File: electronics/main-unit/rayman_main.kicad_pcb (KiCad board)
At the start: 2 copper layers, 88 x 100 mm, 112 parts, among them M1 M1, M2 M2, Q1 BC817, T1A_FUSE2 1808 SMD FUSEHOLDER, U1 ESP32-S3-WROOM-1, U2 SN74AHCT125N, U3 MCP1826S-3302E/DB, U4 SSR-DA41F

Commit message: lamp animation fix
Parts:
- removed AUDIO1: Conn_01x03_Socket, Connector_Audio:Jack_3.5mm_PJ320D_Horizontal
- removed the R21 at (103.6, 98.2)
- added AUDIO_OUT1: Conn_01x03_Socket, Connector_JST:JST_PH_B3B-PH-SM4-TB_1x03-1MP_P2.00mm_Vertical, F.Cu at (76.4, 83.6)
- added R33: 220R, Resistor_SMD:R_0805_2012Metric, B.Cu at (95.0, 36.6)
- added R34: 220R, Resistor_SMD:R_0805_2012Metric, B.Cu at (113.2, 66.7)
- R40: renamed from R29; value 1k -> 10k
- R41: renamed from R26; value 2k2 -> 22k
- moved R31 2.18 mm to (102.8, 98.2)
- moved R30 1.36 mm to (99.0, 98.2)
- moved R7 1.19 mm to (141.1, 36.4)
- moved C6 0.91 mm to (130.2, 38.0)
- moved C7 0.59 mm to (130.2, 35.5)
- renumbered C4 to C10, C5 to C11, C23 to C12, C24 to C13, C12 to C14, C22 to C15, C8 to C16, C9 to C17, C7 to C18, C16 to C19, C15 to C2, C17 to C20, C18 to C21, C19 to C22, C10 to C23, C11 to C24, C20 to C4, C2 to C5, C13 to C6, C14 to C7, C6 to C8, C21 to C9, D15 to D1, D8 to D10, D3 to D11, D11 to D12, D7 to D14, D12 to D15, D14 to D16, D16 to D2, D9 to D3, D10 to D4, D4 to D5, D5 to D7, D1 to D8, D2 to D9, R35 to R1, R14 to R12, R8 to R13, R15 to R14, R40 to R15, R12 to R16, R13 to R17, R42 to R18, R20 to R19, R7 to R2, R31 to R20, R32 to R21, R37 to R22, R3 to R23, R1 to R24, R38 to R25, R25 to R26, R39 to R27, R4 to R28, R24 to R29, R5 to R3, R17 to R30, R18 to R31, R19 to R32, R2 to R35, R28 to R36, R27 to R37, R16 to R38, R30 to R39, R36 to R4, R33 to R42, R34 to R43, R41 to R5, R22 to R6, R23 to R7, R6 to R8, T1A_FUSE2 to T1A_FUSE1, U4 to U3, U3 to U4
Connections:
- PROG1 pad MP: GND -> (no net)
- R19 pad 1: Net-(U1-IO14) -> Net-(U2-4A)
- RJ_LED1 pad 8: GND -> Net-(R33-Pad1)
- TF1 pad G1: GND -> unconnected-(TF1-PadG1)
- TF1 pad G2: GND -> unconnected-(TF1-PadG2)
- TF1 pad G3: GND -> unconnected-(TF1-PadG3)
- TF1 pad G4: GND -> unconnected-(TF1-PadG4)
- U1 pad 38: unconnected-(U1-IO2-Pad38) -> io2
- U2 pad 11: Net-(U2-4Y) -> unconnected-(U2-4Y-Pad11)
- U2 pad 12: Net-(U1-IO14) -> Net-(U2-4A)
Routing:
- net Net-(R33-Pad1): track 0.00 -> 122.4 mm, vias 0 -> 1
- net Net-(R34-Pad1): track 25.4 -> 77.5 mm, vias 0 -> 1
- net Net-(U1-IO14): track 58.7 -> 22.2 mm, vias 3 -> 2
- net Net-(U2-4Y): track 28.5 -> 0.00 mm
- net io2: track 0.00 -> 24.6 mm, vias 0 -> 2
- net Net-(U2-4A): track 0.00 -> 13.6 mm, vias 0 -> 1
- net Net-(DF_MUSIC1-DAC_L): track 63.1 -> 71.3 mm, vias 1 -> 0
- net Net-(audio_out1-DO): track 9.40 -> 14.7 mm
- net GND: track 65.9 -> 63.8 mm
- net Net-(U2-2Y): track 14.4 -> 13.2 mm
- net +3V3: track 306.6 -> 305.7 mm, vias 10 -> 9
- net Net-(R31-Pad2): track 35.0 -> 34.1 mm
- net Net-(TB1-BIN1): track 91.1 -> 90.4 mm
- net Net-(U2-1Y): track 10.3 -> 9.69 mm
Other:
- board text added: "Rev 1.5 25-MAR-2026"
- board text removed: "Rev 1.4 27-JAN-2026"

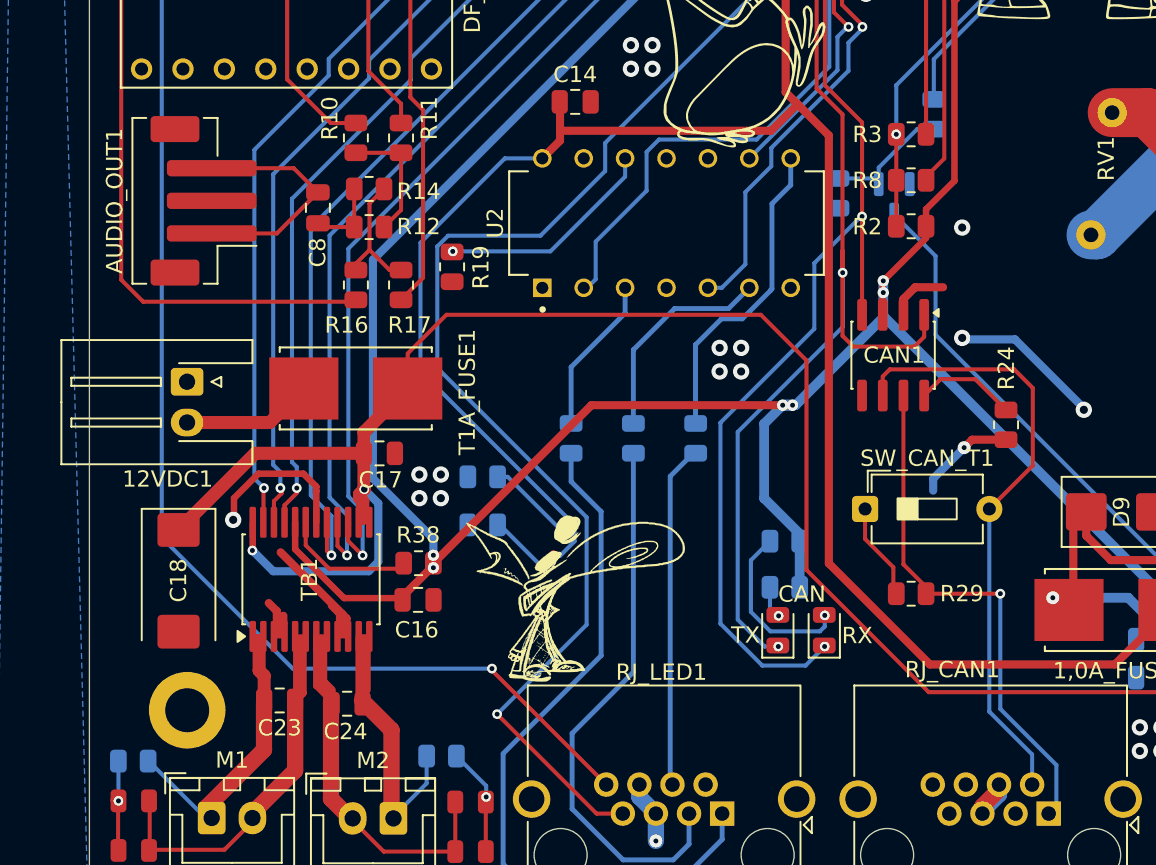
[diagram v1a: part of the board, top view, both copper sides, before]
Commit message: lamp fans control added; uv boost anims added; ambiente light timeout fixed
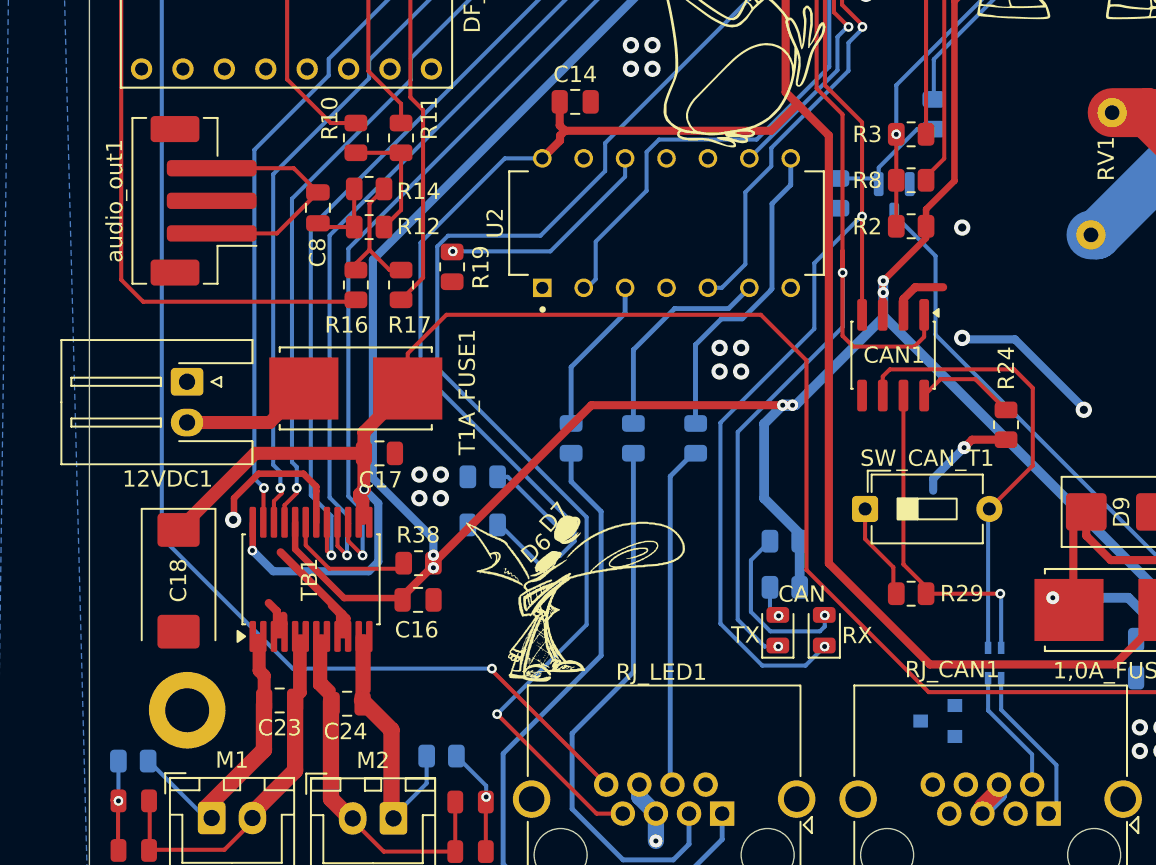
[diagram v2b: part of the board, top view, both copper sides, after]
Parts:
- added D17: PESD1CAN, moja:SOT23-3, B.Cu at (121.5, 115.5)
- added FL1: ACM2012-900-2P-T001, moja:FIL_ACM2012-900-2P-T001, B.Cu at (125.0, 112.0)
- D6, D7: footprint LED_SMD:LED_0402_1005Metric -> LED_SMD:LED_0201_0603Metric
- renumbered AUDIO_OUT1 to audio_out1
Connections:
- RJ_CAN1 pad 1: Net-(CAN1-CANH) -> Net-(FL1-Pad1)
- RJ_CAN1 pad 2: Net-(CAN1-CANL) -> Net-(FL1-Pad2)
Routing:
- net Net-(CAN1-CANH): track 31.7 -> 20.0 mm
- net Net-(FL1-Pad1): track 0.00 -> 9.92 mm
- net Net-(CAN1-CANL): track 37.5 -> 28.1 mm
- net Net-(FL1-Pad2): track 0.00 -> 7.65 mm
- net +5V: track 179.6 -> 180.1 mm

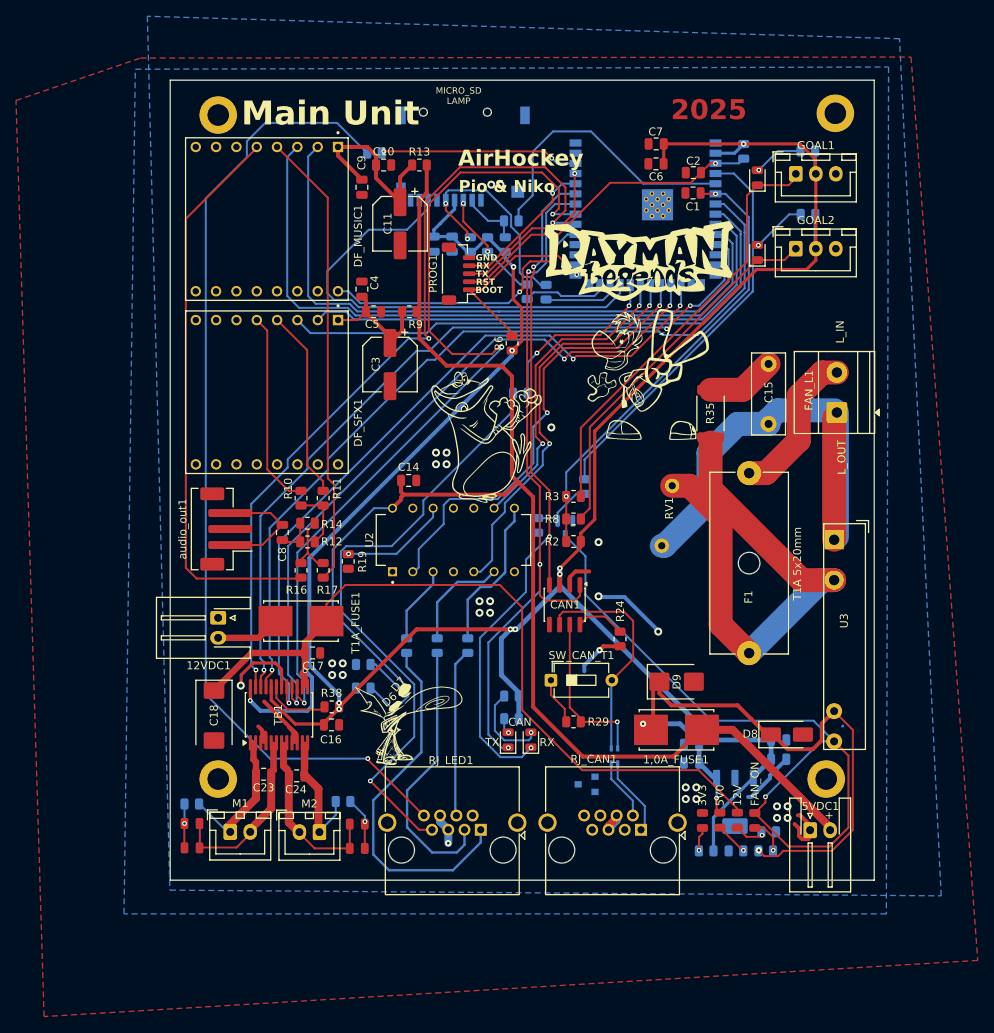
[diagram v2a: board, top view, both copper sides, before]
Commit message: fail safe added to lamp fans
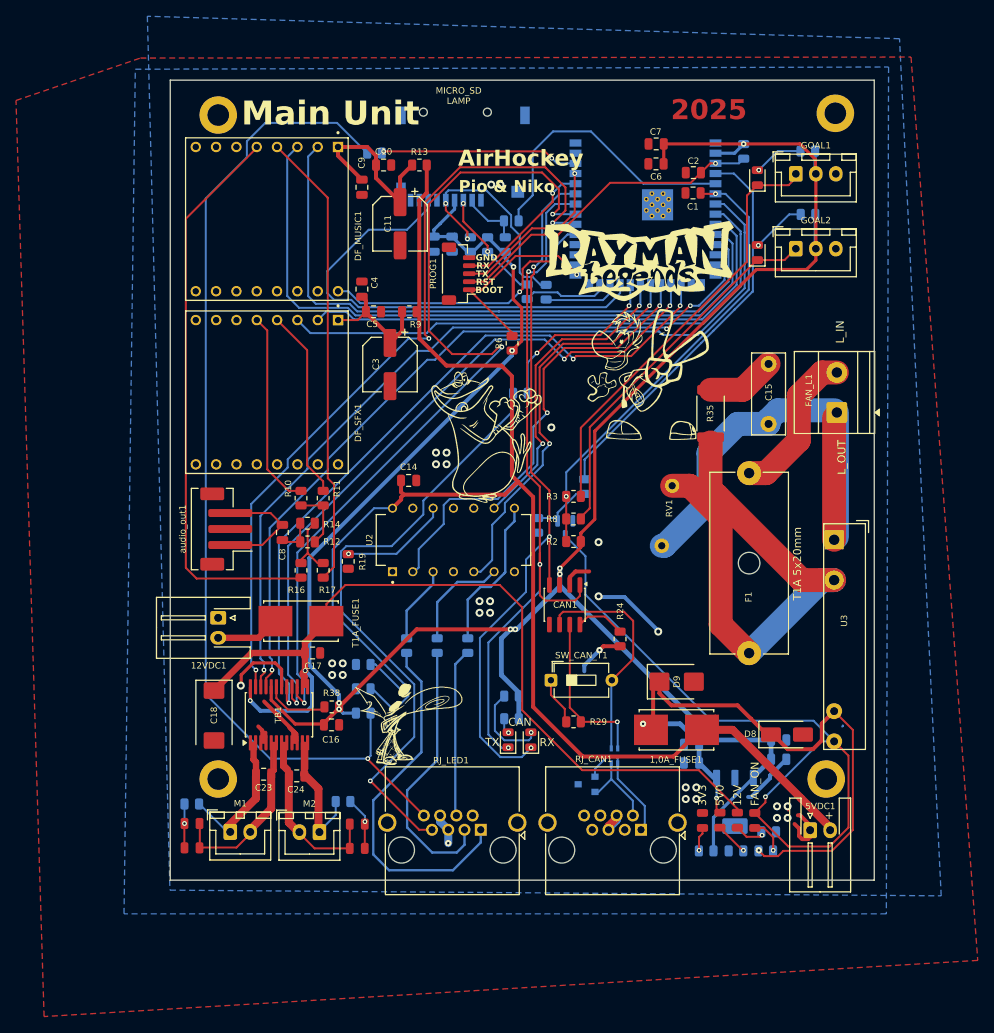
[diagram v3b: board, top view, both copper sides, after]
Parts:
- added R44: 10K, Resistor_SMD:R_0805_2012Metric, B.Cu at (93.6, 106.7)
- moved R36 0.09 mm to (93.6, 103.6)
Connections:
- D17 pad 1: Net-(CAN1-CANH) -> Net-(D17-Pad1)
- D17 pad 2: Net-(CAN1-CANL) -> Net-(D17-Pad2)
- FL1 pad 1: Net-(FL1-Pad1) -> Net-(D17-Pad1)
- FL1 pad 2: Net-(FL1-Pad2) -> Net-(D17-Pad2)
- RJ_CAN1 pad 1: Net-(FL1-Pad1) -> Net-(D17-Pad1)
- RJ_CAN1 pad 2: Net-(FL1-Pad2) -> Net-(D17-Pad2)
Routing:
- net Net-(D17-Pad1): track 0.00 -> 15.0 mm
- net Net-(D17-Pad2): track 0.00 -> 10.4 mm
- net Net-(FL1-Pad1): track 9.92 -> 0.00 mm
- net Net-(FL1-Pad2): track 7.65 -> 0.00 mm
- net Net-(R33-Pad1): track 122.4 -> 128.2 mm
- net +3V3: track 305.7 -> 308.0 mm
